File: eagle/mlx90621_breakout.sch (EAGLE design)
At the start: 16 parts, among them J1 ARDUINO_R3_SHIELD

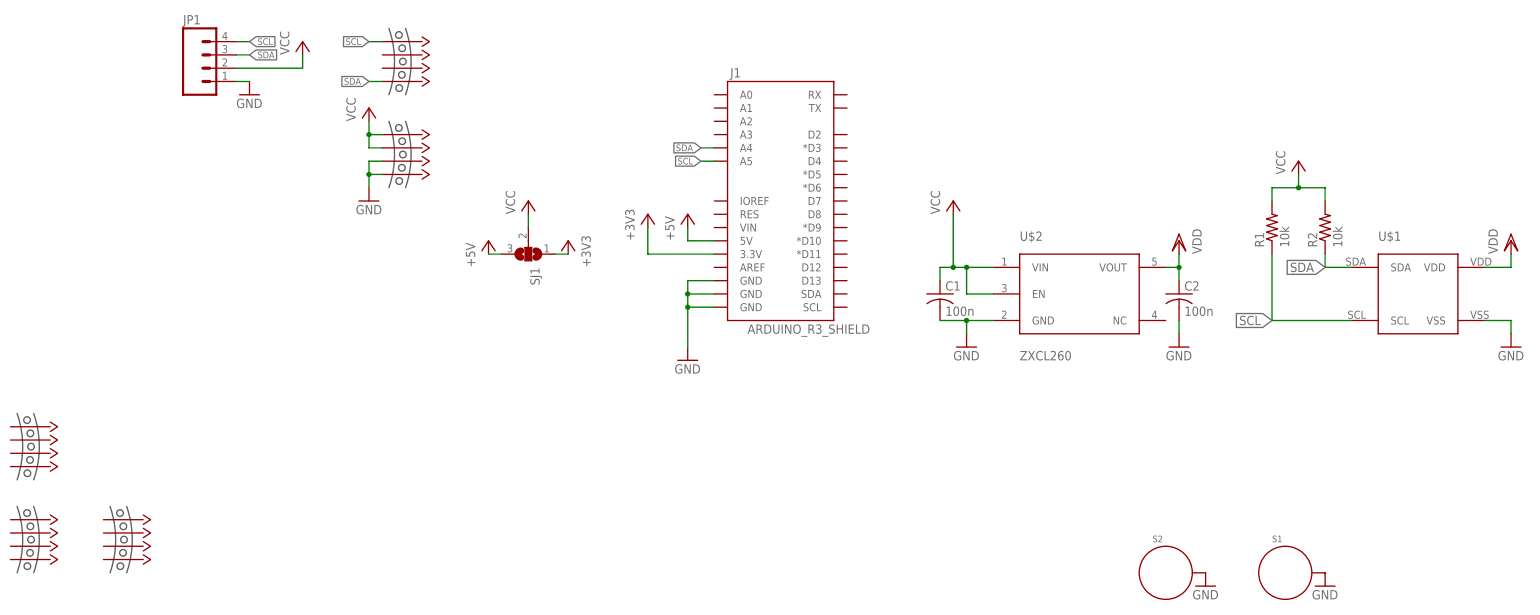
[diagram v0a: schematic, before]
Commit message: cleaned breakout for better component counting at BOM generation
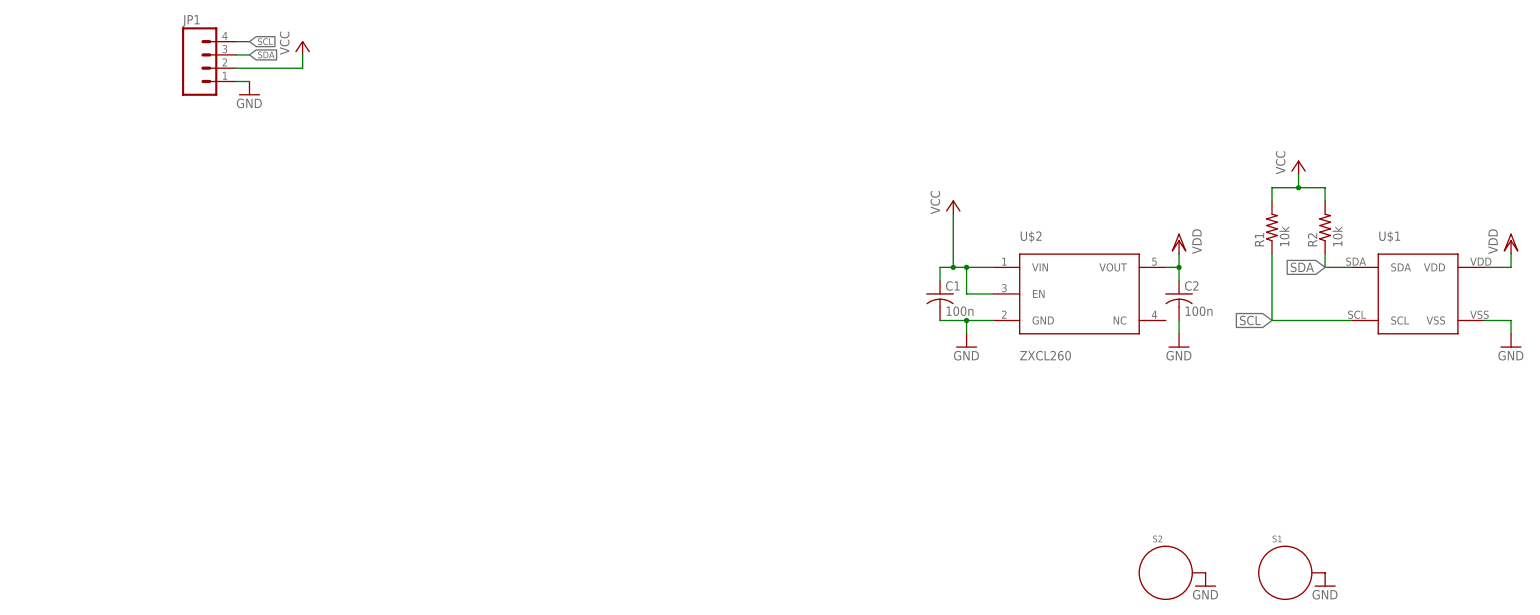
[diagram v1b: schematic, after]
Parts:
- removed J1: ARDUINO_R3_SHIELD, SparkFun-Boards:ARDUINO_R3_SHIELD
- removed SJ1: (no value), jumper:SJ2W
- removed U$3, U$4, U$5, U$6, U$7: MOUSE-BITES-4, mouse-bites:MOUSE-BITES-4
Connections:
- removed net +3V3: J1.3.3V, SJ1.1
- removed net +5V: J1.5V, SJ1.3
- net GND: no longer J1.GND@0, J1.GND@1, J1.GND@2, U$4.3, U$4.4
- net SCL: no longer J1.A5, U$3.1
- net SDA: no longer J1.A4, U$3.4
- net VCC: no longer SJ1.2, U$4.1, U$4.2
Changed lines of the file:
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@@
 <?xml version="1.0" encoding="utf-8"?>
 <!DOCTYPE eagle SYSTEM "eagle.dtd">
-<eagle version="7.3.0">
+<eagle version="9.0.1">
 <drawing>
 <settings>
 <setting alwaysvectorfont="no"/>
+<setting keepoldvectorfont="yes"/>
 <setting verticaltext="up"/>
 </settings>
@@
 </classes>
 <parts>
-<part name="J1" library="SparkFun-Boards" deviceset="ARDUINO_R3_SHIELD" device=""/>
 <part name="FRAME1" library="frames" deviceset="A3L-LOC" device=""/>
 <part name="C1" library="adafruit" deviceset="C-US" device="C0603" value="100n"/>
@@
 <part name="VDD2" library="supply1" deviceset="VDD" device=""/>
 <part name="GND3" library="SparkFun-Aesthetics" deviceset="GND" device=""/>
-<part name="P+3" library="supply1" deviceset="VCC" device=""/>
-<part name="GND4" library="SparkFun-Aesthetics" deviceset="GND" device=""/>
-<part name="SJ1" library="jumper" deviceset="SJ2W" device=""/>
-<part name="P+4" library="supply1" deviceset="+5V" device=""/>
-<part name="P+5" library="supply1" deviceset="+5V" device=""/>
-<part name="+3V1" library="supply1" deviceset="+3V3" device=""/>
-<part name="+3V2" library="supply1" deviceset="+3V3" device=""/>
 <part name="S1" library="SparkFun-Electromechanical" deviceset="STANDOFF_ELECTRICAL" device=""/>
 <part name="S2" library="SparkFun-Electromechanical" deviceset="STANDOFF_ELECTRICAL" device=""/>
@@
 <part name="GND7" library="SparkFun-Aesthetics" deviceset="GND" device=""/>
 <part name="P+6" library="supply1" deviceset="VCC" device=""/>
-<part name="U$3" library="mouse-bites" deviceset="MOUSE-BITES-4" device=""/>
-<part name="U$4" library="mouse-bites" deviceset="MOUSE-BITES-4" device=""/>
-<part name="GND8" library="SparkFun-Aesthetics" deviceset="GND" device=""/>
-<part name="P+7" library="supply1" deviceset="VCC" device=""/>
-<part name="U$5" library="mouse-bites" deviceset="MOUSE-BITES-4" device=""/>
-<part name="U$6" library="mouse-bites" deviceset="MOUSE-BITES-4" device=""/>
-<part name="U$7" library="mouse-bites" deviceset="MOUSE-BITES-4" device=""/>
 </parts>
 <sheets>
@@
 </plain>
 <instances>
-<instance part="J1" gate="G$1" x="228.6" y="86.36"/>
 <instance part="FRAME1" gate="G$1" x="0" y="0"/>
 <instance part="C1" gate="G$1" x="259.08" y="66.04"/>
@@
 <instance part="VDD2" gate="G$1" x="368.3" y="76.2"/>
 <instance part="GND3" gate="1" x="368.3" y="55.88"/>
-<instance part="P+3" gate="VCC" x="180.34" y="83.82"/>
-<instance part="GND4" gate="1" x="210.82" y="53.34"/>
-<instance part="SJ1" gate="G$1" x="180.34" y="73.66" rot="R270"/>
-<instance part="P+4" gate="1" x="172.72" y="76.2"/>
-<instance part="P+5" gate="1" x="210.82" y="81.28"/>
-<instance part="+3V1" gate="G$1" x="187.96" y="76.2" rot="MR0"/>
-<instance part="+3V2" gate="G$1" x="203.2" y="81.28"/>
 <instance part="S1" gate="G$1" x="325.12" y="12.7"/>
 <instance part="S2" gate="G$1" x="302.26" y="12.7"/>
@@
 <instance part="GND7" gate="1" x="127" y="104.14"/>
 <instance part="P+6" gate="VCC" x="137.16" y="114.3"/>
-<instance part="U$3" gate="G$1" x="152.4" y="116.84"/>
-<instance part="U$4" gate="G$1" x="152.4" y="99.06"/>
-<instance part="GND8" gate="1" x="149.86" y="83.82"/>
-<instance part="P+7" gate="VCC" x="149.86" y="101.6"/>
-<instance part="U$5" gate="G$1" x="81.28" y="43.18"/>
-<instance part="U$6" gate="G$1" x="81.28" y="25.4"/>
-<instance part="U$7" gate="G$1" x="99.06" y="25.4"/>
 </instances>
 <busses>
@@
 </segment>
 <segment>
-<pinref part="J1" gate="G$1" pin="GND@0"/>
-<pinref part="GND4" gate="1" pin="GND"/>
-<wire x1="215.9" y1="63.5" x2="210.82" y2="63.5" width="0.1524" layer="91"/>
-<wire x1="210.82" y1="63.5" x2="210.82" y2="55.88" width="0.1524" layer="91"/>
-<pinref part="J1" gate="G$1" pin="GND@1"/>
-<wire x1="215.9" y1="66.04" x2="210.82" y2="66.04" width="0.1524" layer="91"/>
-<wire x1="210.82" y1="66.04" x2="210.82" y2="63.5" width="0.1524" layer="91"/>
-<junction x="210.82" y="63.5"/>
-<pinref part="J1" gate="G$1" pin="GND@2"/>
-<wire x1="215.9" y1="68.58" x2="210.82" y2="68.58" width="0.1524" layer="91"/>
-<wire x1="210.82" y1="68.58" x2="210.82" y2="66.04" width="0.1524" layer="91"/>
-<junction x="210.82" y="66.04"/>
-</segment>
-<segment>
 <pinref part="S2" gate="G$1" pin="P$1"/>
 <pinref part="GND5" gate="1" pin="GND"/>
@@
 <wire x1="124.46" y1="106.68" x2="127" y2="106.68" width="0.1524" layer="91"/>
 <pinref part="GND7" gate="1" pin="GND"/>
-</segment>
-<segment>
-<pinref part="U$4" gate="G$1" pin="3"/>
-<wire x1="152.4" y1="91.44" x2="149.86" y2="91.44" width="0.1524" layer="91"/>
-<pinref part="U$4" gate="G$1" pin="4"/>
-<wire x1="152.4" y1="88.9" x2="149.86" y2="88.9" width="0.1524" layer="91"/>
-<wire x1="149.86" y1="91.44" x2="149.86" y2="88.9" width="0.1524" layer="91"/>
-<pinref part="GND8" gate="1" pin="GND"/>
-<wire x1="149.86" y1="88.9" x2="149.86" y2="86.36" width="0.1524" layer="91"/>
-<junction x="149.86" y="88.9"/>
 </segment>
 </net>
@@
 </segment>
 <segment>
-<pinref part="SJ1" gate="G$1" pin="2"/>
-<pinref part="P+3" gate="VCC" pin="VCC"/>
-<wire x1="180.34" y1="81.28" x2="180.34" y2="78.74" width="0.1524" layer="91"/>
-</segment>
-<segment>
 <pinref part="JP1" gate="G$1" pin="2"/>
 <wire x1="124.46" y1="109.22" x2="137.16" y2="109.22" width="0.1524" layer="91"/>
 <wire x1="137.16" y1="109.22" x2="137.16" y2="111.76" width="0.1524" layer="91"/>
 <pinref part="P+6" gate="VCC" pin="VCC"/>
-</segment>
-<segment>
-<pinref part="U$4" gate="G$1" pin="2"/>
-<wire x1="152.4" y1="93.98" x2="149.86" y2="93.98" width="0.1524" layer="91"/>
-<pinref part="U$4" gate="G$1" pin="1"/>
-<wire x1="152.4" y1="96.52" x2="149.86" y2="96.52" width="0.1524" layer="91"/>
-<wire x1="149.86" y1="93.98" x2="149.86" y2="96.52" width="0.1524" layer="91"/>
-<pinref part="P+7" gate="VCC" pin="VCC"/>
-<wire x1="149.86" y1="96.52" x2="149.86" y2="99.06" width="0.1524" layer="91"/>
-<junction x="149.86" y="96.52"/>
 </segment>
 </net>
@@
 </segment>
 <segment>
-<pinref part="J1" gate="G$1" pin="A4"/>
-<wire x1="215.9" y1="93.98" x2="213.36" y2="93.98" width="0.1524" layer="91"/>
-<label x="213.36" y="93.98" size="1.27" layer="95" rot="R180" xref="yes"/>
-</segment>
-<segment>
 <pinref part="JP1" gate="G$1" pin="3"/>
 <wire x1="124.46" y1="111.76" x2="127" y2="111.76" width="0.1524" layer="91"/>
 <label x="127" y="111.76" size="1.27" layer="95" xref="yes"/>
-</segment>
-<segment>
-<pinref part="U$3" gate="G$1" pin="4"/>
-<wire x1="152.4" y1="106.68" x2="149.86" y2="106.68" width="0.1524" layer="91"/>
-<label x="149.86" y="106.68" size="1.27" layer="95" rot="R180" xref="yes"/>
 </segment>
 </net>
@@
 </segment>
 <segment>
-<pinref part="J1" gate="G$1" pin="A5"/>
-<wire x1="215.9" y1="91.44" x2="213.36" y2="91.44" width="0.1524" layer="91"/>
-<label x="213.36" y="91.44" size="1.27" layer="95" rot="R180" xref="yes"/>
-</segment>
-<segment>
 <pinref part="JP1" gate="G$1" pin="4"/>
 <wire x1="124.46" y1="114.3" x2="127" y2="114.3" width="0.1524" layer="91"/>
 <label x="127" y="114.3" size="1.27" layer="95" xref="yes"/>
 </segment>
-<segment>
-<pinref part="U$3" gate="G$1" pin="1"/>
-<wire x1="152.4" y1="114.3" x2="149.86" y2="114.3" width="0.1524" layer="91"/>
-<label x="149.86" y="114.3" size="1.27" layer="95" rot="R180" xref="yes"/>
-</segment>
-</net>
-<net name="+3V3" class="0">
-<segment>
-<pinref part="J1" gate="G$1" pin="3.3V"/>
-<pinref part="+3V2" gate="G$1" pin="+3V3"/>
-<wire x1="203.2" y1="78.74" x2="203.2" y2="73.66" width="0.1524" layer="91"/>
-<wire x1="203.2" y1="73.66" x2="215.9" y2="73.66" width="0.1524" layer="91"/>
-</segment>
-<segment>
-<pinref part="SJ1" gate="G$1" pin="1"/>
-<pinref part="+3V1" gate="G$1" pin="+3V3"/>
-<wire x1="187.96" y1="73.66" x2="185.42" y2="73.66" width="0.1524" layer="91"/>
-</segment>
-</net>
-<net name="+5V" class="0">
-<segment>
-<pinref part="SJ1" gate="G$1" pin="3"/>
-<pinref part="P+4" gate="1" pin="+5V"/>
-<wire x1="172.72" y1="73.66" x2="175.26" y2="73.66" width="0.1524" layer="91"/>
-</segment>
-<segment>
-<pinref part="J1" gate="G$1" pin="5V"/>
-<pinref part="P+5" gate="1" pin="+5V"/>
-<wire x1="210.82" y1="78.74" x2="210.82" y2="76.2" width="0.1524" layer="91"/>
-<wire x1="210.82" y1="76.2" x2="215.9" y2="76.2" width="0.1524" layer="91"/>
-</segment>
-</net>
+</net>

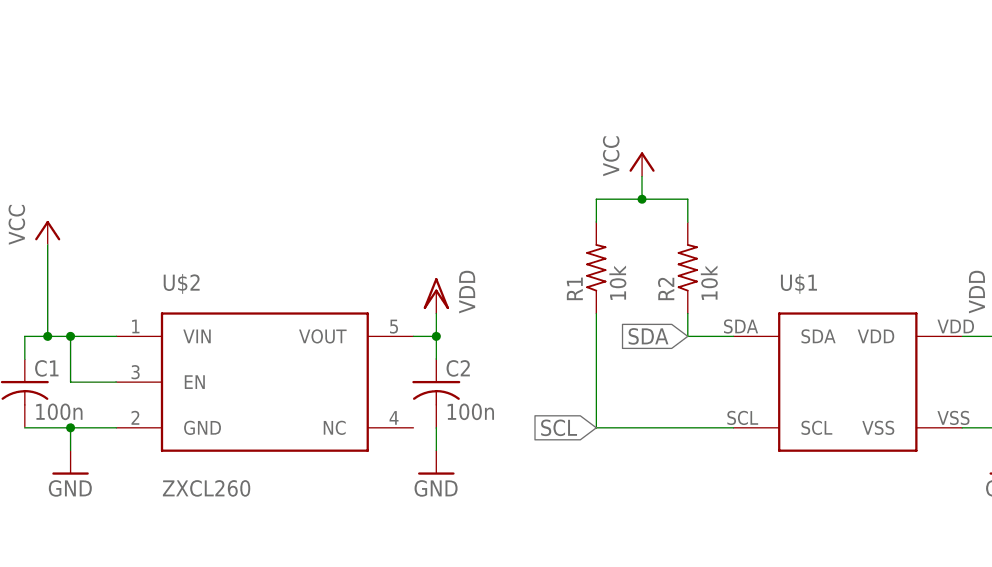
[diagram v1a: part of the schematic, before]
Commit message: changed References for ICs (U1, U2)
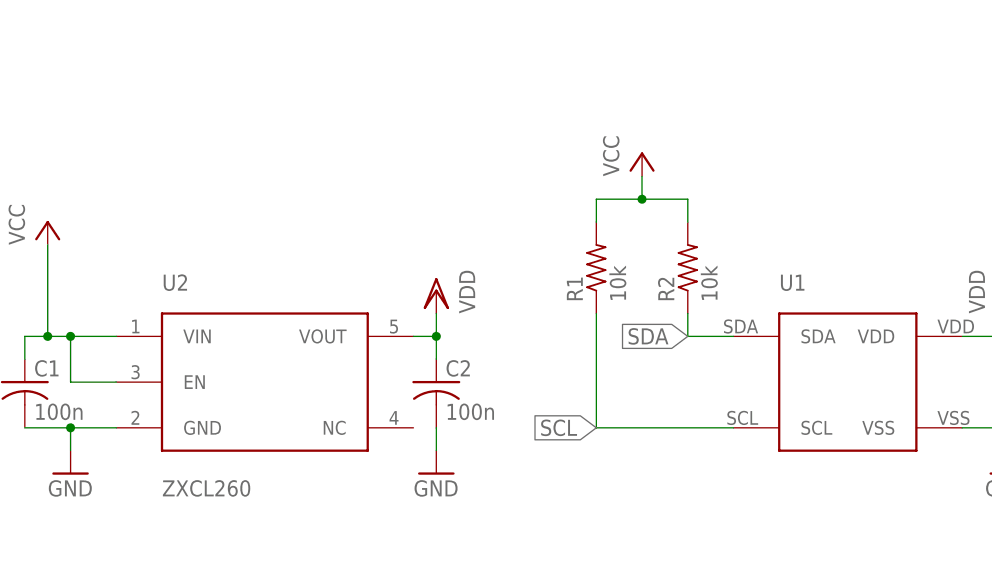
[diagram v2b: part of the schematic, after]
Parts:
- renumbered U$1 to U1, U$2 to U2
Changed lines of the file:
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@@
 <part name="R1" library="adafruit" deviceset="R-US_" device="R0603" value="10k"/>
 <part name="R2" library="adafruit" deviceset="R-US_" device="R0603" value="10k"/>
-<part name="U$1" library="melexis" deviceset="MLX90621" device="BAD"/>
-<part name="U$2" library="melexis" deviceset="ZXCL260" device=""/>
+<part name="U1" library="melexis" deviceset="MLX90621" device="BAD"/>
+<part name="U2" library="melexis" deviceset="ZXCL260" device=""/>
 <part name="GND1" library="SparkFun-Aesthetics" deviceset="GND" device=""/>
 <part name="VDD1" library="supply1" deviceset="VDD" device=""/>
@@
 <instance part="R1" gate="G$1" x="322.58" y="78.74" rot="R90"/>
 <instance part="R2" gate="G$1" x="332.74" y="78.74" rot="R90"/>
-<instance part="U$1" gate="G$1" x="350.52" y="66.04"/>
-<instance part="U$2" gate="G$1" x="284.48" y="60.96"/>
+<instance part="U1" gate="G$1" x="350.52" y="66.04"/>
+<instance part="U2" gate="G$1" x="284.48" y="60.96"/>
 <instance part="GND1" gate="1" x="264.16" y="55.88"/>
 <instance part="VDD1" gate="G$1" x="304.8" y="76.2" rot="MR0"/>
@@
 <pinref part="GND1" gate="1" pin="GND"/>
 <wire x1="264.16" y1="58.42" x2="264.16" y2="60.96" width="0.1524" layer="91"/>
-<pinref part="U$2" gate="G$1" pin="GND"/>
+<pinref part="U2" gate="G$1" pin="GND"/>
 <wire x1="264.16" y1="60.96" x2="269.24" y2="60.96" width="0.1524" layer="91"/>
 <pinref part="C1" gate="G$1" pin="2"/>
@@
 </segment>
 <segment>
-<pinref part="U$1" gate="G$1" pin="VSS"/>
+<pinref part="U1" gate="G$1" pin="VSS"/>
 <pinref part="GND3" gate="1" pin="GND"/>
 <wire x1="363.22" y1="60.96" x2="368.3" y2="60.96" width="0.1524" layer="91"/>
@@
 <net name="VCC" class="0">
 <segment>
-<pinref part="U$2" gate="G$1" pin="VIN"/>
+<pinref part="U2" gate="G$1" pin="VIN"/>
 <pinref part="P+1" gate="VCC" pin="VCC"/>
 <wire x1="269.24" y1="71.12" x2="264.16" y2="71.12" width="0.1524" layer="91"/>
@@
 <wire x1="259.08" y1="71.12" x2="261.62" y2="71.12" width="0.1524" layer="91"/>
 <junction x="261.62" y="71.12"/>
-<pinref part="U$2" gate="G$1" pin="EN"/>
+<pinref part="U2" gate="G$1" pin="EN"/>
 <wire x1="269.24" y1="66.04" x2="264.16" y2="66.04" width="0.1524" layer="91"/>
 <wire x1="264.16" y1="66.04" x2="264.16" y2="71.12" width="0.1524" layer="91"/>
@@
 <net name="VDD" class="0">
 <segment>
-<pinref part="U$2" gate="G$1" pin="VOUT"/>
+<pinref part="U2" gate="G$1" pin="VOUT"/>
 <pinref part="VDD1" gate="G$1" pin="VDD"/>
 <wire x1="302.26" y1="71.12" x2="304.8" y2="71.12" width="0.1524" layer="91"/>
@@
 </segment>
 <segment>
-<pinref part="U$1" gate="G$1" pin="VDD"/>
+<pinref part="U1" gate="G$1" pin="VDD"/>
 <pinref part="VDD2" gate="G$1" pin="VDD"/>
 <wire x1="363.22" y1="71.12" x2="368.3" y2="71.12" width="0.1524" layer="91"/>
@@
 <net name="SDA" class="0">
 <segment>
-<pinref part="U$1" gate="G$1" pin="SDA"/>
+<pinref part="U1" gate="G$1" pin="SDA"/>
 <pinref part="R2" gate="G$1" pin="1"/>
 <wire x1="337.82" y1="71.12" x2="332.74" y2="71.12" width="0.1524" layer="91"/>
@@
 <net name="SCL" class="0">
 <segment>
-<pinref part="U$1" gate="G$1" pin="SCL"/>
+<pinref part="U1" gate="G$1" pin="SCL"/>
 <pinref part="R1" gate="G$1" pin="1"/>
 <wire x1="337.82" y1="60.96" x2="322.58" y2="60.96" width="0.1524" layer="91"/>
